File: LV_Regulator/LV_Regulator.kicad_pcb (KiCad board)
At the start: 4 copper layers, 150 x 100 mm, 195 parts, among them IC1 UCC12040DVE, IC2 MIC29152WU, IC3 MIC29152WU, J1 430450400, J2 430450400, J3 430450800, J4 430450800, J5 SWD, J6 2169890001, K1 41.52.9.005.0010, Q1 BC807, U1 ADM2483xRW, U2 STM32F103C8Tx, U3 25CSM04xxSN, U4 BQ25858QWRRVRQ1, U5 CSD19506KTT, U6 CSD19506KTT, U7 CSD19506KTT, U8 CSD19506KTT, Y1 32.768kHz, Y2 8MHz

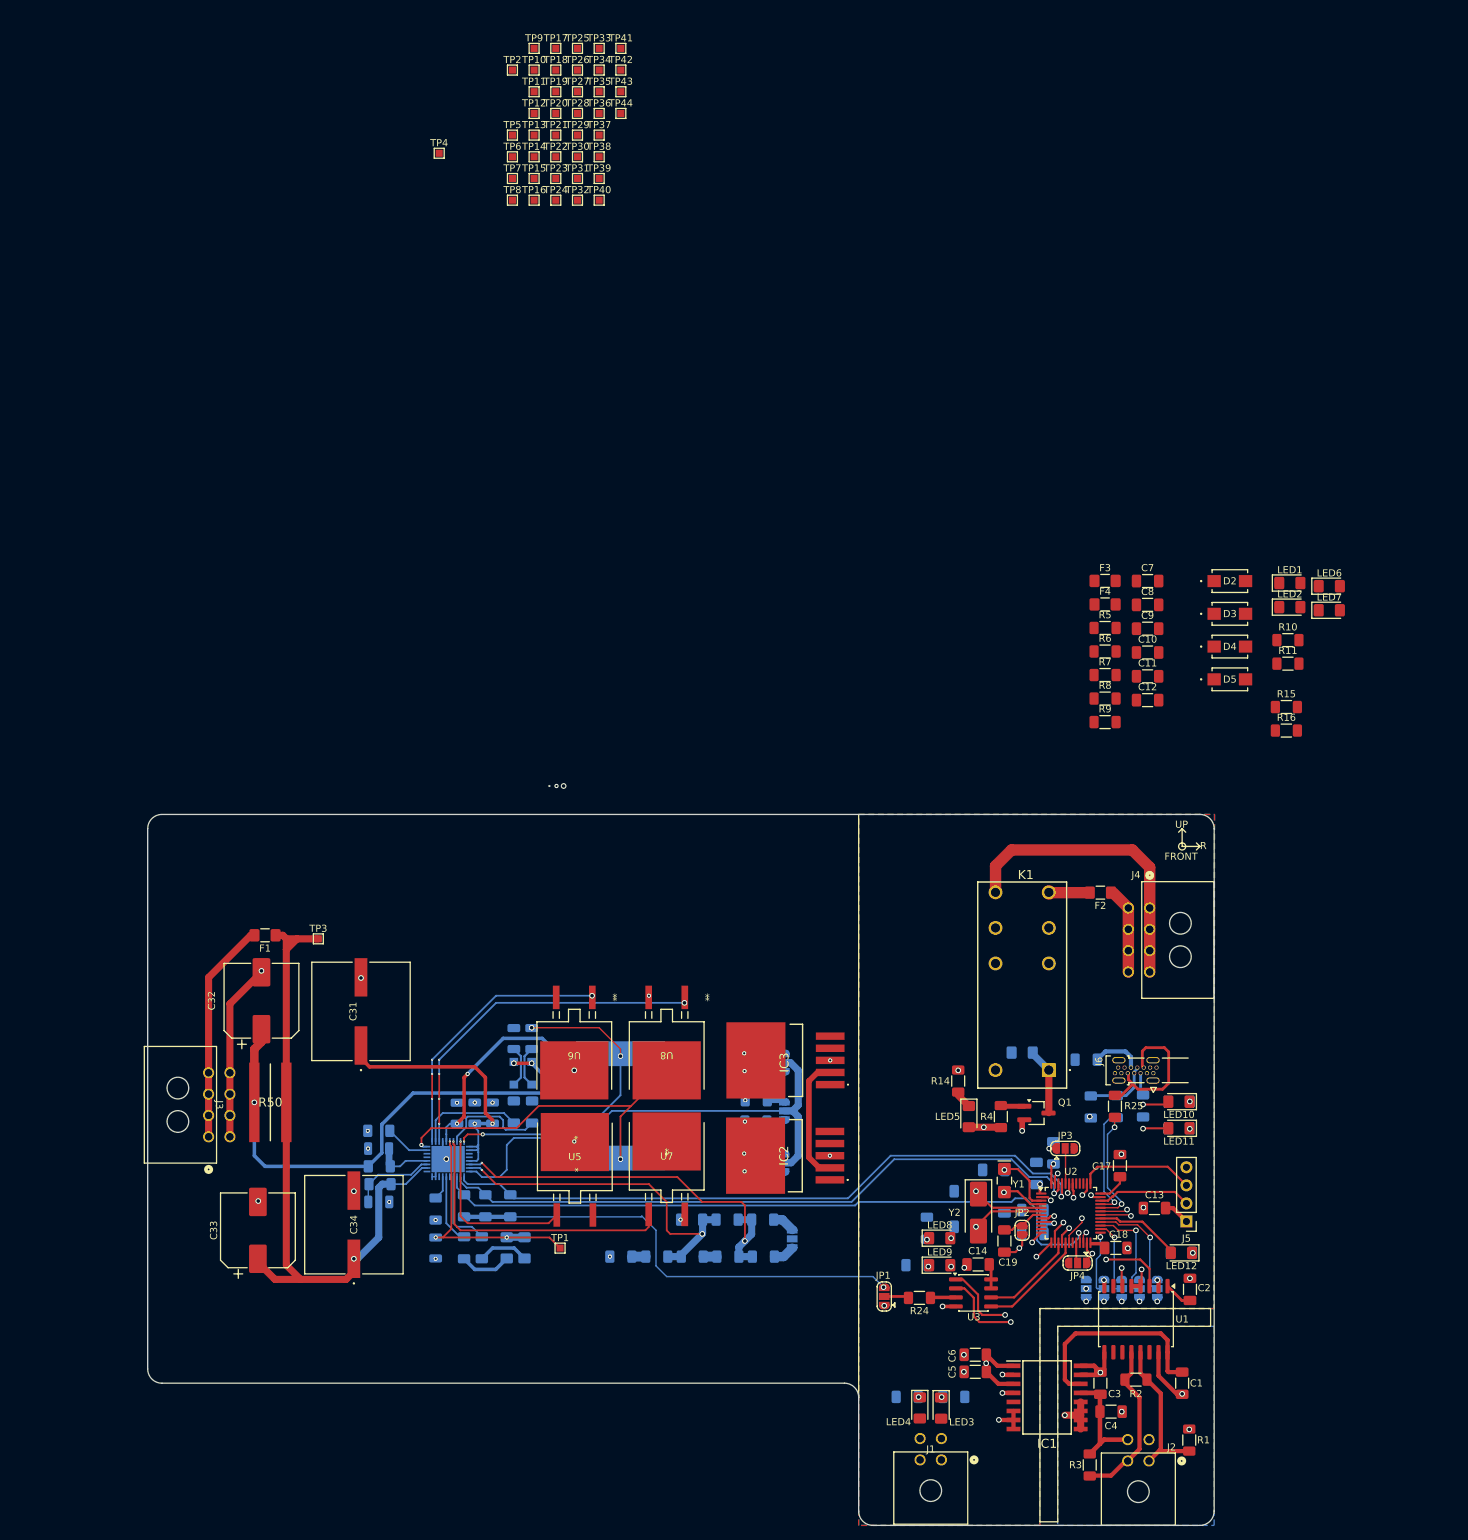
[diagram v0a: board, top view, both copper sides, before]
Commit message: Continued PCB Routing
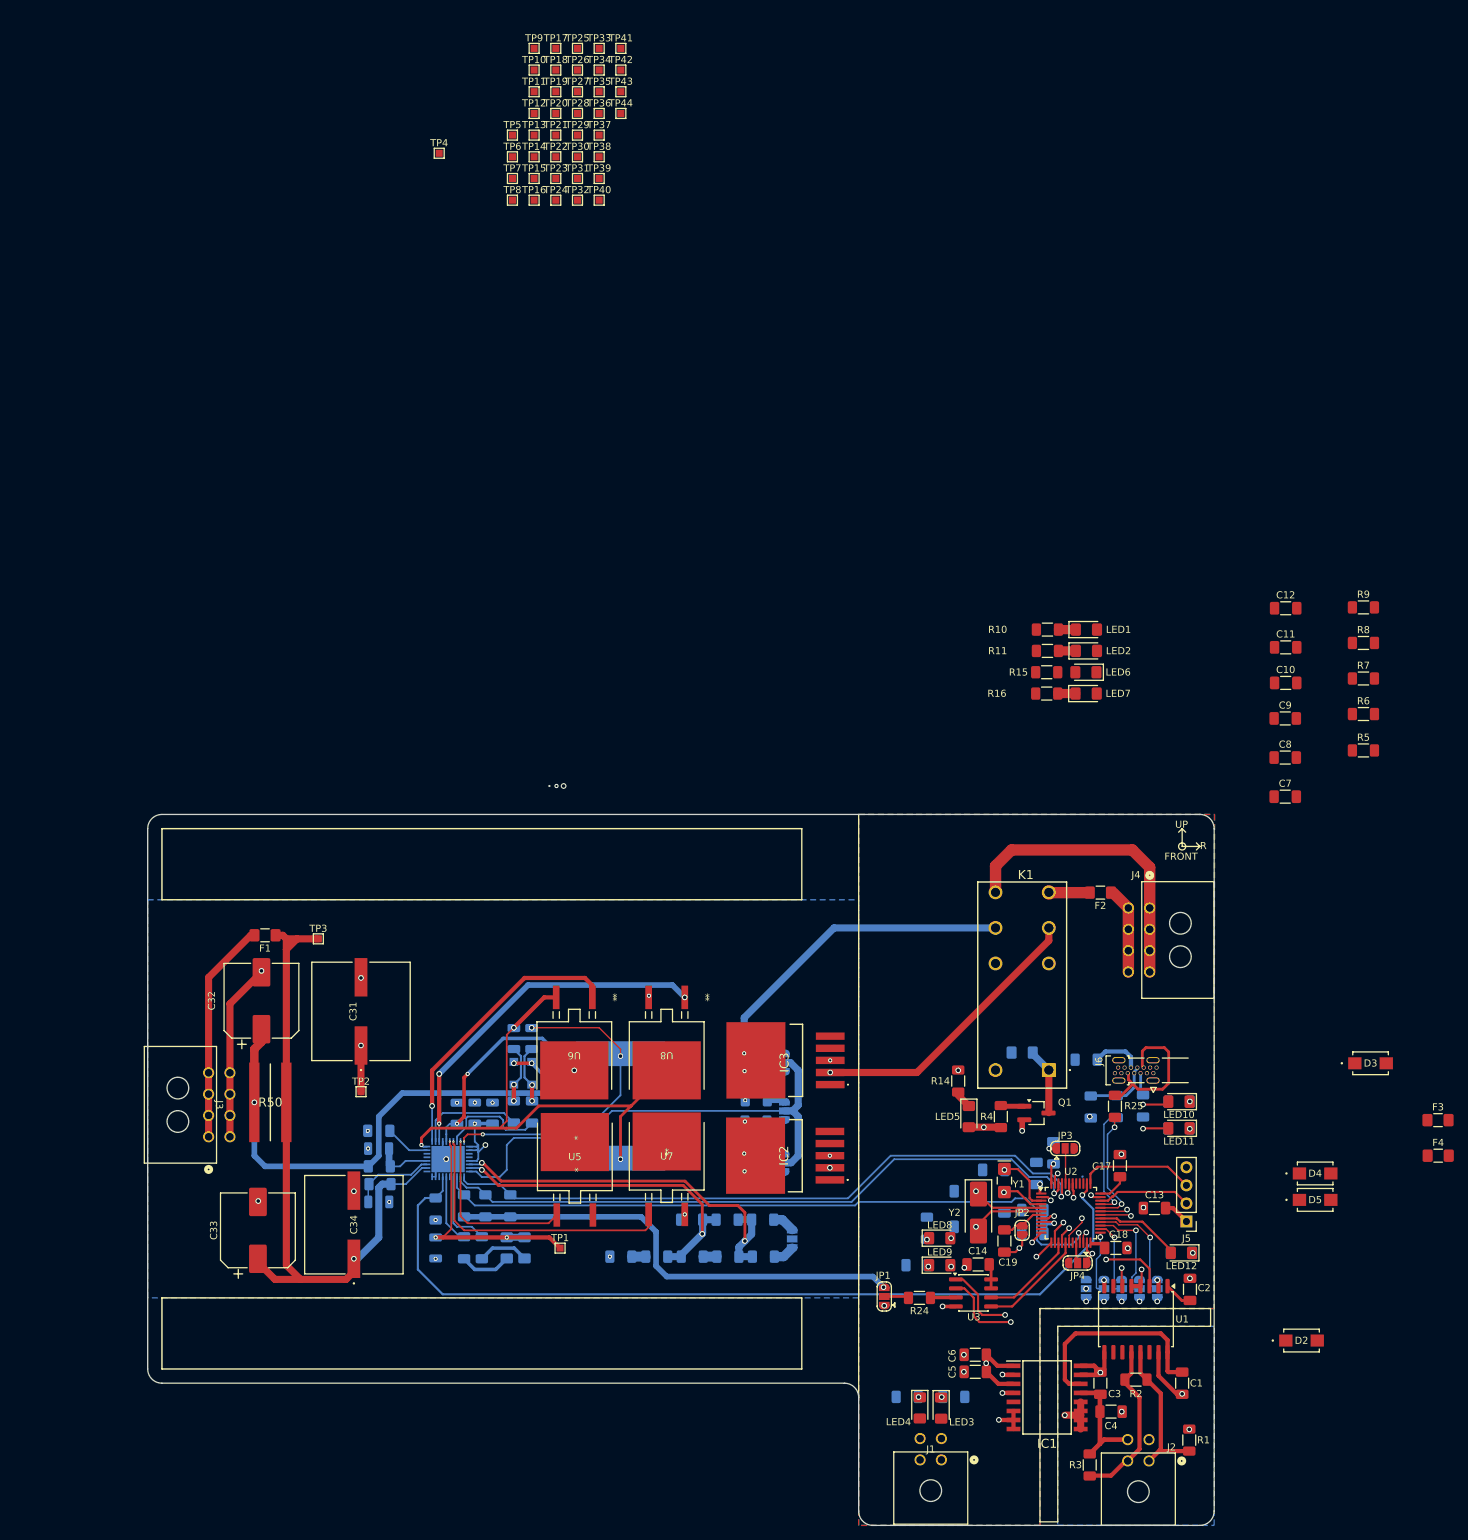
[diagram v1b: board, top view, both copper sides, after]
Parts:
- moved TP2 145.3 mm to (111.0, 83.0)
- moved D2 107.3 mm to (243.3, 118.0)
- moved F4 90.6 mm to (262.5, 92.0)
- moved F3 89.1 mm to (262.5, 87.0)
- moved D4 75.1 mm to (245.2, 94.5)
- moved D5 74.2 mm to (245.2, 98.2)
- moved D3 66.2 mm to (253.0, 79.0)
- moved R5 40.2 mm to (252.0, 35.0)
- moved R9 39.8 mm to (252.0, 14.9)
- moved R6 37.4 mm to (252.0, 29.9)
- moved R8 37.2 mm to (252.0, 19.9)
- moved R7 36.3 mm to (252.0, 24.9)
- moved LED6 36.3 mm to (213.0, 24.0), turned to 180 degrees
- moved LED7 36.1 mm to (213.0, 27.0)
- moved C7 36.0 mm to (241.0, 41.5)
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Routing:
- net CE_N: track 5.30 -> 123.9 mm
- net GND: track 55.0 -> 100.6 mm
- net SW2: track 48.4 -> 71.1 mm, vias 2 -> 3
- net SYS: track 57.0 -> 60.5 mm, vias 3 -> 5
- net Net-(LED7-K): track 0.00 -> 2.51 mm
- net Net-(LED2-K): track 0.00 -> 2.45 mm
- net Net-(LED1-K): track 0.00 -> 2.45 mm
- net HIDRV2_FET4: track 37.7 -> 40.0 mm, vias 4 -> 1
- net Net-(D7-K): track 5.83 -> 8.13 mm, vias 0 -> 2
- net Net-(D6-K): track 5.91 -> 8.15 mm, vias 0 -> 2
- net Net-(U6-D): track 72.1 -> 73.5 mm
- net LODRV2_FET3: track 49.3 -> 49.9 mm, vias 5 -> 3
- net ACUV: track 56.1 -> 55.5 mm
- added copper zone on In2.Cu, net SYS

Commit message: PCB routing and TP placement
Finished first PCB routing and started TP placement
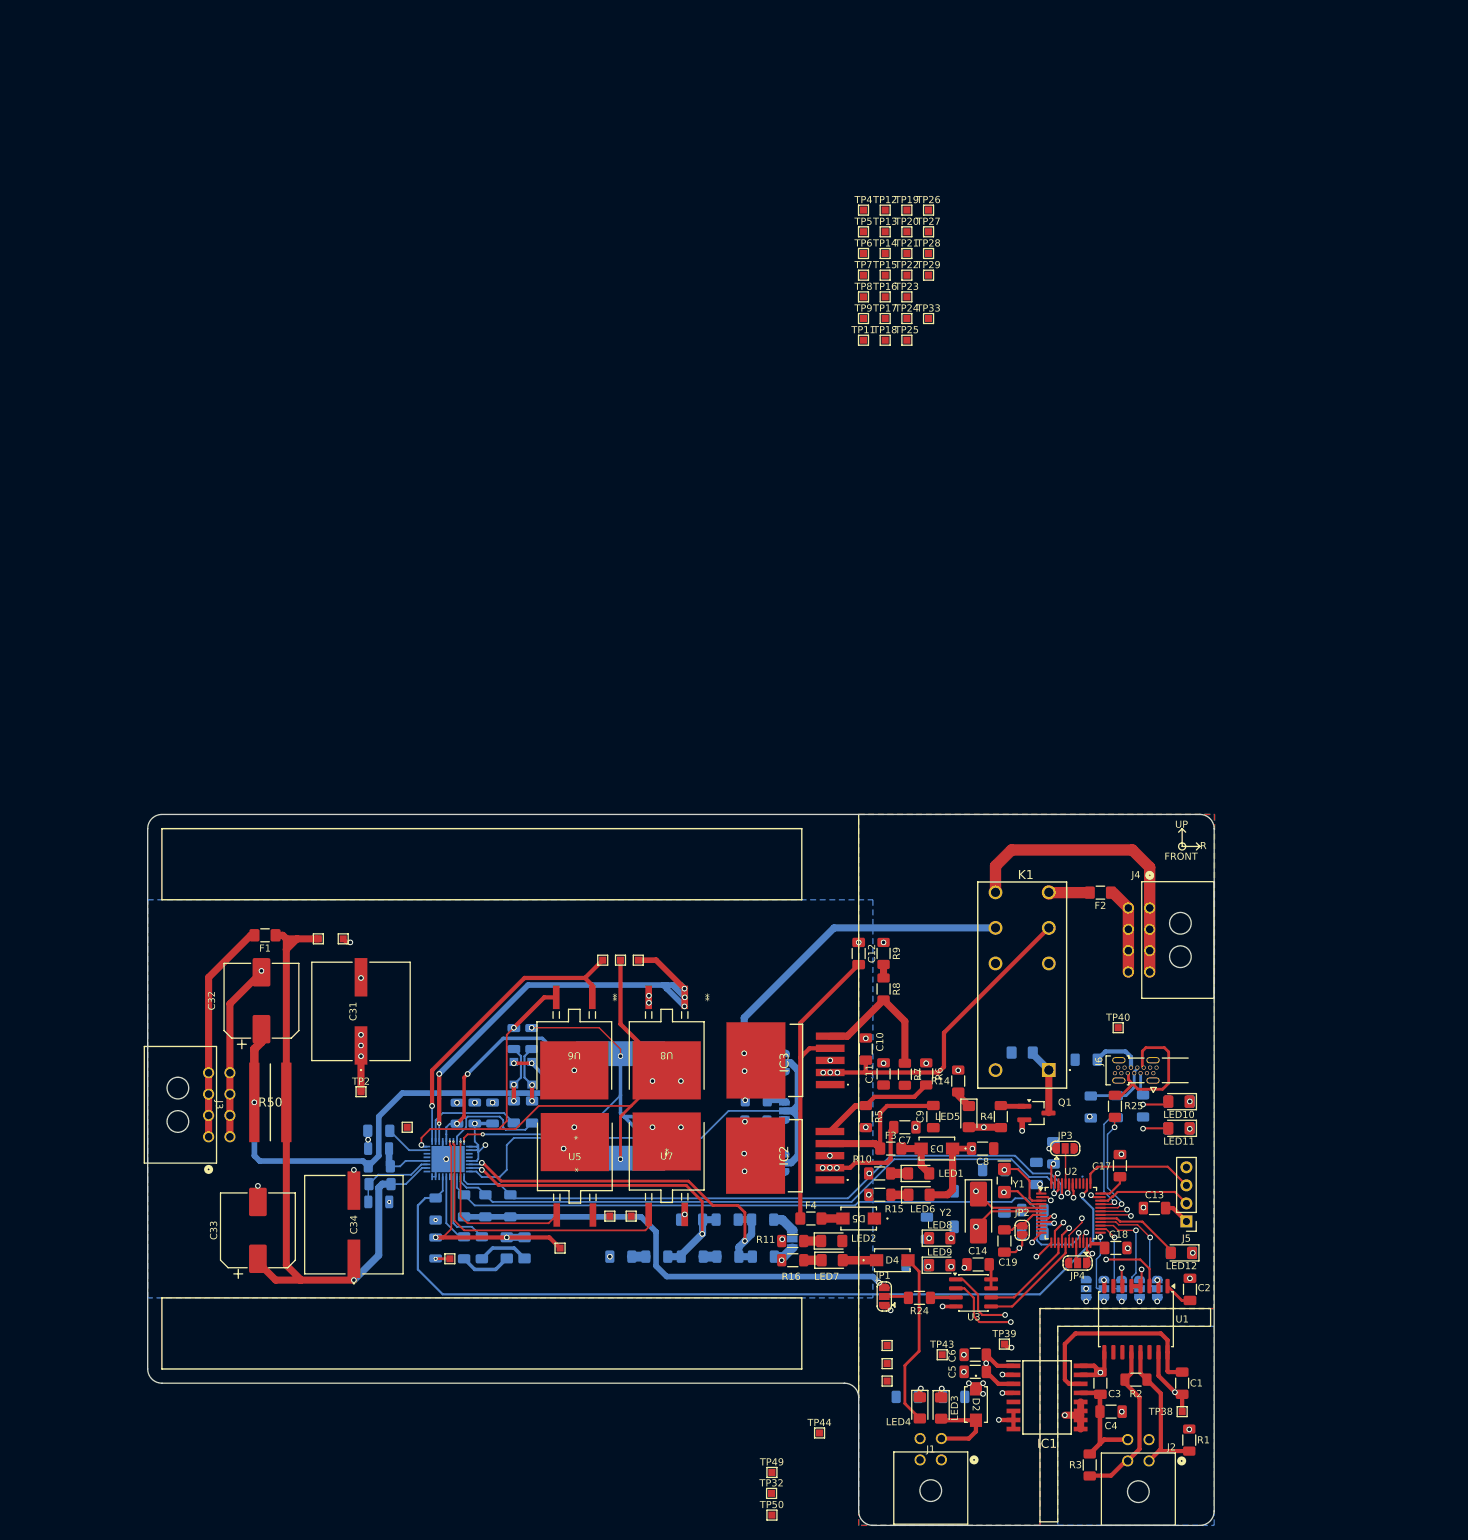
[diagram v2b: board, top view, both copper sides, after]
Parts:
- added TP46: TestPoint, TestPoint:TestPoint_Pad_1.0x1.0mm, F.Cu at (185.0, 123.7)
- added TP47: TestPoint, TestPoint:TestPoint_Pad_1.0x1.0mm, F.Cu at (185.0, 118.7)
- added TP49: TestPoint, TestPoint:TestPoint_Pad_1.0x1.0mm, F.Cu at (168.8, 136.6)
- added TP50: TestPoint, TestPoint:TestPoint_Pad_1.0x1.0mm, F.Cu at (168.8, 142.6)
- TP10: value TestPoint -> SW2
- TP11: value TestPoint -> RS485-TX TP
- TP12: value TestPoint -> RS485-RX TP
- TP13: value TestPoint -> I2C-SCL TP
- TP14: value TestPoint -> I2C-SDA TP
- TP15: value TestPoint -> INT-N TP
- TP2: value TestPoint -> SYS TP
- TP38: value TestPoint -> Isolated Ground
- TP39, TP40, TP41, TP42, TP43, TP44: value TestPoint -> Ground
- TP4: value TestPoint -> 12V BAT+
- TP5: value TestPoint -> V_OUT_SNS REG
- TP6: value TestPoint -> 3V3_VBAT
- TP7: value TestPoint -> ACUV TP
- TP8: value TestPoint -> ACOV TP
- TP9: value TestPoint -> SW1
- moved TP38 194.6 mm to (226.5, 128.0)
- moved TP44 187.7 mm to (175.5, 131.0)
- moved TP32 183.9 mm to (168.8, 139.5)
- moved TP43 183.3 mm to (192.8, 120.0)
- moved TP37 177.5 mm to (185.0, 121.2)
- moved TP39 173.6 mm to (201.5, 118.5)
- moved TP42 168.9 mm to (123.5, 106.5)
- moved TP35 158.2 mm to (149.0, 100.5)
- moved TP31 146.0 mm to (146.0, 100.5)
- moved TP36 145.1 mm to (117.5, 88.0)
- moved TP40 137.4 mm to (217.5, 74.0)
- moved TP41 131.2 mm to (108.5, 61.5)
- moved TP10 125.8 mm to (147.5, 64.5)
- moved TP34 125.3 mm to (150.0, 64.5)
- moved TP30 113.1 mm to (145.0, 64.5)
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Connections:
- TP10 pad 1: unconnected-(TP10-Pad1) -> SW2
- TP11 pad 1: unconnected-(TP11-Pad1) -> RS485-TX
- TP12 pad 1: unconnected-(TP12-Pad1) -> RS485-RX
- TP13 pad 1: unconnected-(TP13-Pad1) -> I2C_SCL
- TP14 pad 1: unconnected-(TP14-Pad1) -> I2C_SDA
- TP15 pad 1: unconnected-(TP15-Pad1) -> INT_N
- TP16 pad 1: unconnected-(TP16-Pad1) -> ADR1
- TP17 pad 1: unconnected-(TP17-Pad1) -> ADR2
- TP18 pad 1: unconnected-(TP18-Pad1) -> ADR3
- TP19 pad 1: unconnected-(TP19-Pad1) -> ADR4
- TP20 pad 1: unconnected-(TP20-Pad1) -> ADR5
- TP21 pad 1: unconnected-(TP21-Pad1) -> RS485-DIR
- TP22 pad 1: unconnected-(TP22-Pad1) -> RELEJ
- TP23 pad 1: unconnected-(TP23-Pad1) -> MOSI
- TP24 pad 1: unconnected-(TP24-Pad1) -> MISO_DOBROTO
- TP25 pad 1: unconnected-(TP25-Pad1) -> SCK
- TP26 pad 1: unconnected-(TP26-Pad1) -> SS
- TP27 pad 1: unconnected-(TP27-Pad1) -> CE_N
- TP28 pad 1: unconnected-(TP28-Pad1) -> SRN
- TP29 pad 1: unconnected-(TP29-Pad1) -> SRP
- TP30 pad 1: unconnected-(TP30-Pad1) -> HIDRV2_FET4
- TP31 pad 1: unconnected-(TP31-Pad1) -> HIDRV1_FET1
- TP32 pad 1: unconnected-(TP32-Pad1) -> 3V3_EXT
- TP33 pad 1: unconnected-(TP33-Pad1) -> BTST2
- TP34 pad 1: unconnected-(TP34-Pad1) -> LODRV2_FET3
- TP35 pad 1: unconnected-(TP35-Pad1) -> LODRV1_FET2
- TP36 pad 1: unconnected-(TP36-Pad1) -> BTST1
- TP37 pad 1: unconnected-(TP37-Pad1) -> +5V
- TP38 pad 1: unconnected-(TP38-Pad1) -> GND_ISO
- TP4 pad 1: unconnected-(TP4-Pad1) -> BAT+
- TP5 pad 1: unconnected-(TP5-Pad1) -> VOUT
- TP6 pad 1: unconnected-(TP6-Pad1) -> VBAT
- TP7 pad 1: unconnected-(TP7-Pad1) -> ACUV
- TP8 pad 1: unconnected-(TP8-Pad1) -> ACOV
- TP9 pad 1: unconnected-(TP9-Pad1) -> SW1
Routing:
- net Net-(IC3-OUT): track 0.00 -> 43.9 mm
- net 3V3_EXT: track 0.00 -> 24.6 mm
- net Net-(IC2-OUT): track 0.00 -> 20.3 mm
- net Net-(IC3-ADJ): track 0.00 -> 19.8 mm
- net SW2: track 71.1 -> 89.3 mm, vias 3 -> 5
- net SYS: track 60.5 -> 77.7 mm, vias 5 -> 13
- net SW1: track 45.2 -> 61.7 mm, vias 4 -> 6
- net Net-(IC2-ADJ): track 0.00 -> 16.2 mm
- net LODRV2_FET3: track 49.9 -> 64.7 mm, vias 3 -> 5
- net +5V: track 13.0 -> 25.4 mm, vias 2 -> 7
- net 5V_EXT: track 0.00 -> 11.8 mm
- net GND: track 100.6 -> 111.0 mm, vias 45 -> 57
- net 5V_INT: track 0.00 -> 6.76 mm
- net VBAT: track 93.5 -> 98.9 mm
- net HIDRV2_FET4: track 40.0 -> 43.6 mm
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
